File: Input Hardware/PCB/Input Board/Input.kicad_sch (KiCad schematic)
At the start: 4 parts

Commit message: Revert "conflict resolution"
This reverts commit e2196486344c2f16c0f4e50e55e8bad7e306dbb3, reversing
changes made to 6978c7447e140ee759e19aaebffdac22097ec1b9.
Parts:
- SW? (x2): footprint Encoder:Untitled -> Connector_PinHeader_2.54mm:PinHeader_1x05_P2.54mm_Vertical_SMD_Pin1Right
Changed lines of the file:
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@@
 			)
 		)
-		(property "Footprint" "Encoder:Untitled"
+		(property "Footprint" "Connector_PinHeader_2.54mm:PinHeader_1x05_P2.54mm_Vertical_SMD_Pin1Right"
 			(at 88.9 114.3 0)
 			(effects
@@
 			)
 		)
-		(property "Footprint" "Encoder:Untitled"
+		(property "Footprint" "Connector_PinHeader_2.54mm:PinHeader_1x05_P2.54mm_Vertical_SMD_Pin1Right"
 			(at 88.9 50.8 0)
 			(effects

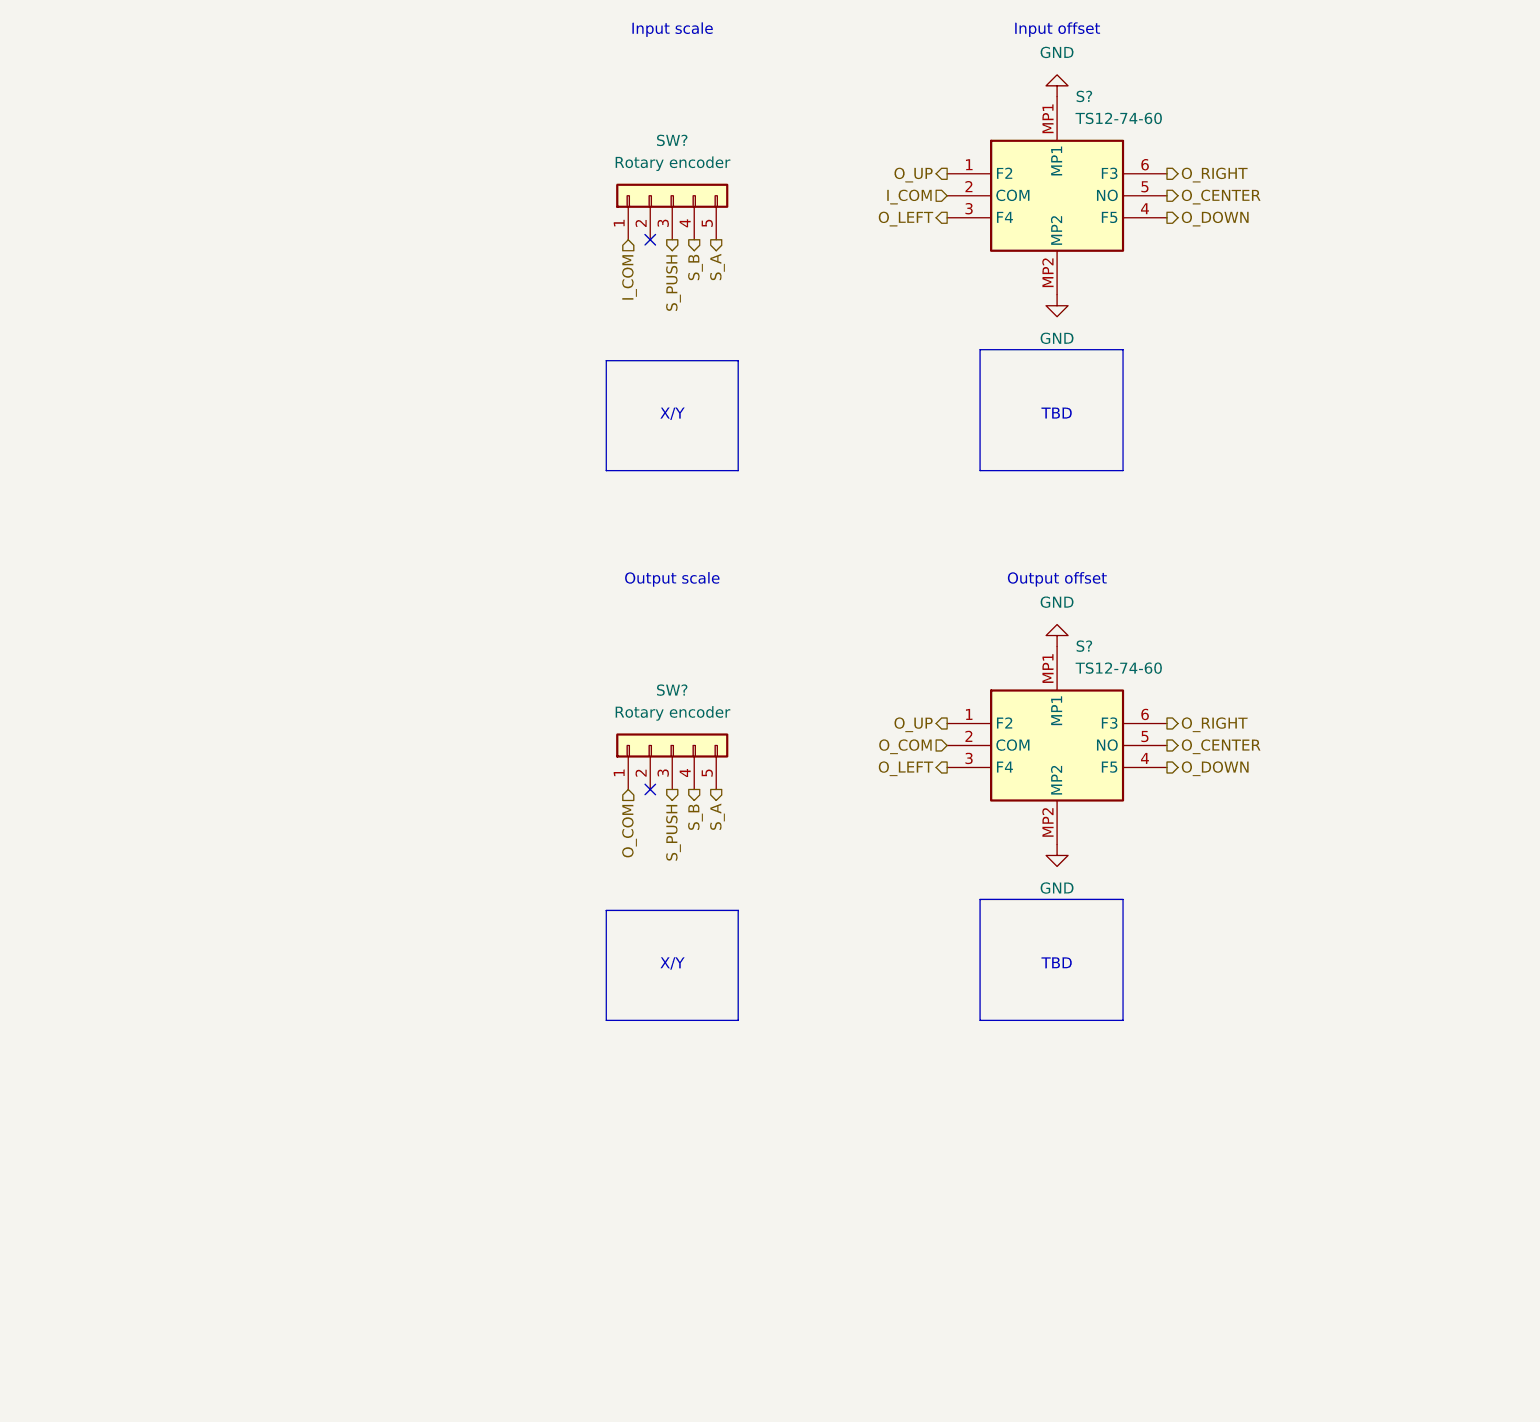
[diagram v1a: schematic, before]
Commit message: Revert "images and pcb stuff"
This reverts commit 6978c7447e140ee759e19aaebffdac22097ec1b9.
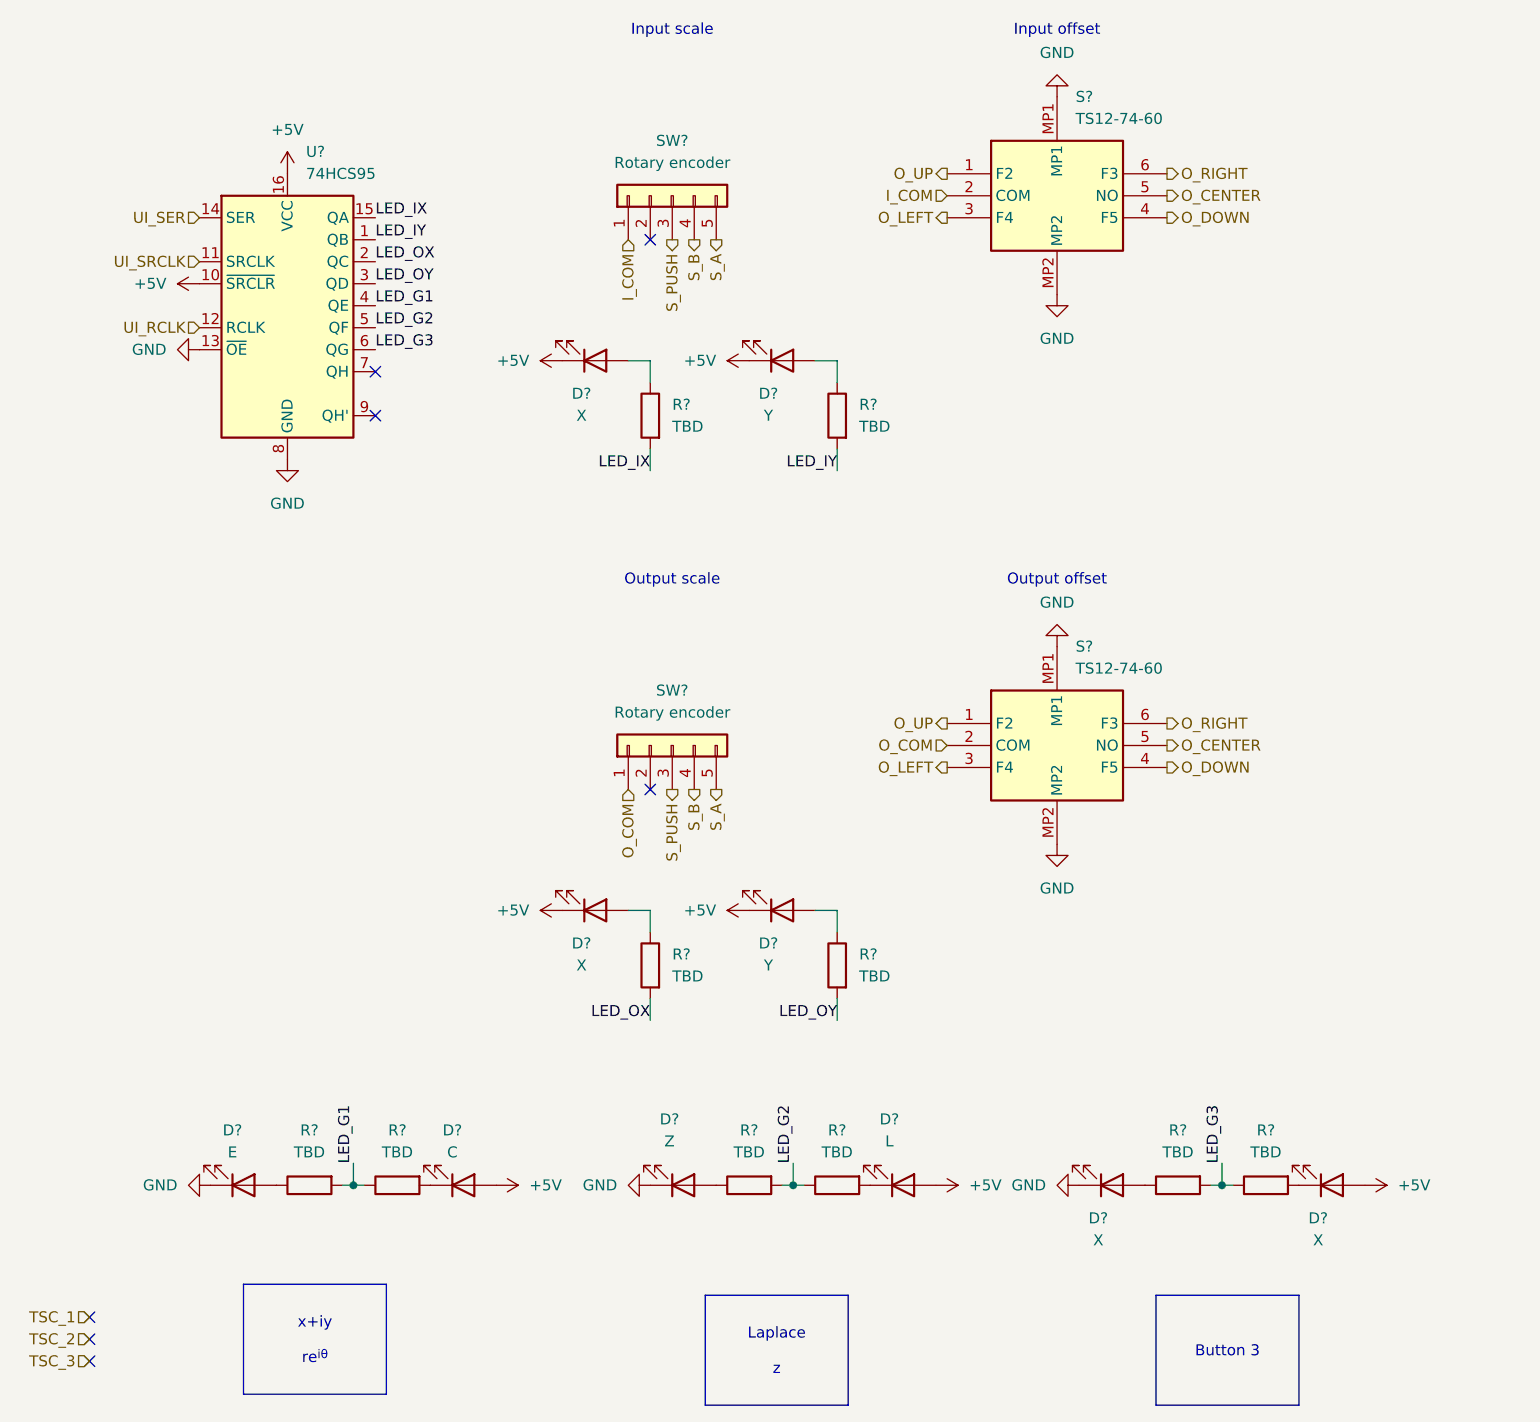
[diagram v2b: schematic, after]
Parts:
- added D? (x4): X, LED_SMD:LED_0603_1608Metric, symbol Device:LED
- added D?: E, LED_SMD:LED_0603_1608Metric, symbol Device:LED
- added D?: L, LED_SMD:LED_0603_1608Metric, symbol Device:LED
- added D?: Z, LED_SMD:LED_0603_1608Metric, symbol Device:LED
- added D? (x2): Y, LED_SMD:LED_0603_1608Metric, symbol Device:LED
- added D?: C, LED_SMD:LED_0603_1608Metric, symbol Device:LED
- added R? (x10): TBD, Resistor_SMD:R_0603_1608Metric, symbol Device:R
- added U?: 74HCS95, symbol 74xx:74HC595
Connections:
- net GND: now also D?.1 (K), D?.1 (K), D?.1 (K), U?.13 (~{OE}), U?.8 (GND)
- new net: D?.2 (A), R?.1 (x7)
- new net: D?.1 (K), R?.2 (x3)
- new net +5V: D?.1 (K), D?.1 (K), D?.1 (K), D?.1 (K), D?.2 (A), D?.2 (A), D?.2 (A), U?.10 (~{SRCLR}), U?.16 (VCC)
- new net LED_G1: R?.1, R?.2, U?.4 (QE)
- new net LED_G2: R?.1, R?.2, U?.5 (QF)
- new net LED_G3: R?.1, R?.2, U?.6 (QG)
- new net LED_IX: R?.2, U?.15 (QA)
- new net LED_IY: R?.2, U?.1 (QB)
- new net LED_OX: R?.2, U?.2 (QC)
- new net LED_OY: R?.2, U?.3 (QD)
- new net UI_RCLK: U?.12 (RCLK)
- new net UI_SER: U?.14 (SER)
- new net UI_SRCLK: U?.11 (SRCLK)
- no-connect marks 2 -> 7
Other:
- note removed: "TBD"
- note removed: "X/Y"

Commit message: stmcube model and fixes
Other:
- note added: "Do you just wanna make all the TBD LED resistors 220/330ohm?"
- note added: "what is this?"
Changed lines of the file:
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@@
 	(generator_version "9.0")
 	(paper "A4")
+	(text "what is this?\n"
+		(exclude_from_sim no)
+		(at 21.59 177.8 0)
+		(effects
+			(font
+				(size 1.27 1.27)
+			)
+		)
+	)
 	(text "Input offset"
 		(exclude_from_sim no)
 		(at 133.35 31.75 0)
+		(effects
+			(font
+				(size 1.27 1.27)
+			)
+		)
+	)
+	(text "Do you just wanna make all the TBD LED resistors 220/330ohm?\n"
+		(exclude_from_sim no)
+		(at 149.86 140.97 0)
 		(effects
 			(font
@@
 	(text "Input scale"
 		(exclude_from_sim no)
-		(at 88.9 31.75 0)
+		(at 88.9 40.64 0)
 		(effects
 			(font
@@
 	(text "Output scale"
 		(exclude_from_sim no)
-		(at 88.9 95.25 0)
+		(at 88.9 104.14 0)
 		(effects
 			(font

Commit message: Footprints
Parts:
- U?: footprint (none) -> Package_SO:SOIC-16_3.9x9.9mm_P1.27mm
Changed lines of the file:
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@@
 			)
 		)
-		(property "Footprint" ""
+		(property "Footprint" "Package_SO:SOIC-16_3.9x9.9mm_P1.27mm"
 			(at 44.45 63.5 0)
 			(effects

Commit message: Fix files idc
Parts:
- added C1101: 100n, Capacitor_SMD:C_0603_1608Metric, symbol Device:C
- gave numbers to parts that had none: 25
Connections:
- net +5V: now also C1101.1
- net GND: now also C1101.2

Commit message: Layout
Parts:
- SW1101, SW1102: footprint Connector_PinHeader_2.54mm:PinHeader_1x05_P2.54mm_Vertical_SMD_Pin1Right -> Encoder:Untitled
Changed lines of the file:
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@@
 			)
 		)
-		(property "Footprint" "Connector_PinHeader_2.54mm:PinHeader_1x05_P2.54mm_Vertical_SMD_Pin1Right"
+		(property "Footprint" "Encoder:Untitled"
 			(at 88.9 114.3 0)
 			(effects
@@
 			)
 		)
-		(property "Footprint" "Connector_PinHeader_2.54mm:PinHeader_1x05_P2.54mm_Vertical_SMD_Pin1Right"
+		(property "Footprint" "Encoder:Untitled"
 			(at 88.9 50.8 0)
 			(effects

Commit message: Filter Amplifier Layout
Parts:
- U1101: value 74HCS95 -> 74HC595
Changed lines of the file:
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@@
 			)
 		)
-		(property "Value" "74HCS95"
+		(property "Value" "74HC595"
 			(at 46.5933 48.26 0)
 			(effects

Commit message: sims and other crap
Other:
- moved on the sheet: D1103, D1106, R1103, R1106
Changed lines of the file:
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@@
 	(wire
 		(pts
-			(xy 83.82 69.85) (xy 86.36 69.85)
+			(xy 88.9 77.47) (xy 91.44 77.47)
 		)
 		(stroke
@@
 	(wire
 		(pts
-			(xy 107.95 69.85) (xy 107.95 72.39)
+			(xy 113.03 77.47) (xy 113.03 80.01)
 		)
 		(stroke
@@
 	(wire
 		(pts
-			(xy 86.36 69.85) (xy 86.36 72.39)
+			(xy 91.44 77.47) (xy 91.44 80.01)
 		)
 		(stroke
@@
 	(wire
 		(pts
-			(xy 86.36 82.55) (xy 86.36 80.01)
+			(xy 91.44 90.17) (xy 91.44 87.63)
 		)
 		(stroke
@@
 	(wire
 		(pts
-			(xy 107.95 82.55) (xy 107.95 80.01)
+			(xy 113.03 90.17) (xy 113.03 87.63)
 		)
 		(stroke
@@
 	(wire
 		(pts
-			(xy 105.41 69.85) (xy 107.95 69.85)
+			(xy 110.49 77.47) (xy 113.03 77.47)
 		)
 		(stroke
@@
 	)
 	(label "LED_IX"
-		(at 86.36 82.55 180)
+		(at 91.44 90.17 180)
 		(effects
 			(font
@@
 	)
 	(label "LED_IY"
-		(at 107.95 82.55 180)
+		(at 113.03 90.17 180)
 		(effects
 			(font
@@
 	(symbol
 		(lib_id "Device:R")
-		(at 107.95 76.2 0)
+		(at 113.03 83.82 0)
 		(mirror y)
 		(unit 1)
@@
 		(fields_autoplaced yes)
 		(property "Reference" "R1106"
-			(at 110.49 74.9301 0)
+			(at 115.57 82.5501 0)
 			(effects
 				(font
@@
 		)
 		(property "Value" "TBD"
-			(at 110.49 77.4701 0)
+			(at 115.57 85.0901 0)
 			(effects
 				(font
@@
 		)
 		(property "Footprint" "Resistor_SMD:R_0603_1608Metric"
-			(at 109.728 76.2 90)
+			(at 114.808 83.82 90)
 			(effects
 				(font
@@
 		)
 		(property "Datasheet" "~"
-			(at 107.95 76.2 0)
+			(at 113.03 83.82 0)
 			(effects
 				(font
@@
 		)
 		(property "Description" "Resistor"
-			(at 107.95 76.2 0)
+			(at 113.03 83.82 0)
 			(effects
 				(font
@@
 	(symbol
 		(lib_id "Device:LED")
-		(at 80.01 69.85 0)
+		(at 85.09 77.47 0)
 		(mirror x)
 		(unit 1)
@@
 		(fields_autoplaced yes)
 		(property "Reference" "D1103"
-			(at 78.4225 73.66 0)
+			(at 83.5025 81.28 0)
 			(effects
 				(font
@@
 		)
 		(property "Value" "X"
-			(at 78.4225 76.2 0)
+			(at 83.5025 83.82 0)
 			(effects
 				(font
@@
 		)
 		(property "Footprint" "LED_SMD:LED_0603_1608Metric"
-			(at 80.01 69.85 0)
+			(at 85.09 77.47 0)
 			(effects
 				(font
@@
 		)
 		(property "Datasheet" "~"
-			(at 80.01 69.85 0)
+			(at 85.09 77.47 0)
 			(effects
 				(font
@@
 		)
 		(property "Description" "Light emitting diode"
-			(at 80.01 69.85 0)
+			(at 85.09 77.47 0)
 			(effects
 				(font
@@
 		)
 		(property "Sim.Pins" "1=K 2=A"
-			(at 80.01 69.85 0)
+			(at 85.09 77.47 0)
 			(effects
 				(font
@@
 	(symbol
 		(lib_id "Device:R")
-		(at 86.36 76.2 0)
+		(at 91.44 83.82 0)
 		(mirror y)
 		(unit 1)
@@
 		(fields_autoplaced yes)
 		(property "Reference" "R1103"
-			(at 88.9 74.9301 0)
+			(at 93.98 82.5501 0)
 			(effects
 				(font
@@
 		)
 		(property "Value" "TBD"
-			(at 88.9 77.4701 0)
+			(at 93.98 85.0901 0)
 			(effects
 				(font
@@
 		)
 		(property "Footprint" "Resistor_SMD:R_0603_1608Metric"
-			(at 88.138 76.2 90)
+			(at 93.218 83.82 90)
 			(effects
 				(font
@@
 		)
 		(property "Datasheet" "~"
-			(at 86.36 76.2 0)
+			(at 91.44 83.82 0)
 			(effects
 				(font
@@
 		)
 		(property "Description" "Resistor"
-			(at 86.36 76.2 0)
+			(at 91.44 83.82 0)
 			(effects
 				(font
@@
 	(symbol
 		(lib_id "power:+5V")
-		(at 76.2 69.85 90)
+		(at 81.28 77.47 90)
 		(unit 1)
 		(exclude_from_sim no)
@@
 		(fields_autoplaced yes)
 		(property "Reference" "#PWR01109"
-			(at 80.01 69.85 0)
+			(at 85.09 77.47 0)
 			(effects
 				(font
@@
 		)
 		(property "Value" "+5V"
-			(at 72.39 69.8499 90)
+			(at 77.47 77.4699 90)
 			(effects
 				(font
@@
 		)
 		(property "Footprint" ""
-			(at 76.2 69.85 0)
+			(at 81.28 77.47 0)
 			(effects
 				(font
@@
 		)
 		(property "Datasheet" ""
-			(at 76.2 69.85 0)
+			(at 81.28 77.47 0)
 			(effects
 				(font
@@
 		)
 		(property "Description" "Power symbol creates a global label with name \"+5V\""
-			(at 76.2 69.85 0)
+			(at 81.28 77.47 0)
 			(effects
 				(font
@@
 	(symbol
 		(lib_id "power:+5V")
-		(at 97.79 69.85 90)
+		(at 102.87 77.47 90)
 		(unit 1)
 		(exclude_from_sim no)
@@
 		(fields_autoplaced yes)
 		(property "Reference" "#PWR01112"
-			(at 101.6 69.85 0)
+			(at 106.68 77.47 0)
 			(effects
 				(font
@@
 		)
 		(property "Value" "+5V"
-			(at 93.98 69.8499 90)
+			(at 99.06 77.4699 90)
 			(effects
 				(font
@@
 		)
 		(property "Footprint" ""
-			(at 97.79 69.85 0)
+			(at 102.87 77.47 0)
 			(effects
 				(font
@@
 		)
 		(property "Datasheet" ""
-			(at 97.79 69.85 0)
+			(at 102.87 77.47 0)
 			(effects
 				(font
@@
 		)
 		(property "Description" "Power symbol creates a global label with name \"+5V\""
-			(at 97.79 69.85 0)
+			(at 102.87 77.47 0)
 			(effects
 				(font
@@
 	(symbol
 		(lib_id "Device:LED")
-		(at 101.6 69.85 0)
+		(at 106.68 77.47 0)
 		(mirror x)
 		(unit 1)
@@
 		(fields_autoplaced yes)
 		(property "Reference" "D1106"
-			(at 100.0125 73.66 0)
+			(at 105.0925 81.28 0)
 			(effects
 				(font
@@
 		)
 		(property "Value" "Y"
-			(at 100.0125 76.2 0)
+			(at 105.0925 83.82 0)
 			(effects
 				(font
@@
 		)
 		(property "Footprint" "LED_SMD:LED_0603_1608Metric"
-			(at 101.6 69.85 0)
+			(at 106.68 77.47 0)
 			(effects
 				(font
@@
 		)
 		(property "Datasheet" "~"
-			(at 101.6 69.85 0)
+			(at 106.68 77.47 0)
 			(effects
 				(font
@@
 		)
 		(property "Description" "Light emitting diode"
-			(at 101.6 69.85 0)
+			(at 106.68 77.47 0)
 			(effects
 				(font
@@
 		)
 		(property "Sim.Pins" "1=K 2=A"
-			(at 101.6 69.85 0)
+			(at 106.68 77.47 0)
 			(effects
 				(font
